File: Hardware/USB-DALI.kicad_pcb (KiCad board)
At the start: 2 copper layers, 71.3 x 25.4 mm, 43 parts, among them J1 USB_A, J2 ST-LINK, J3 Screw_Terminal_01x02, J4 PWR BUS+, J5 PWR BUS-, Q1 BCX56, U1 STM32F103C8T6, U2 PC817, U3 PC817, U4 AMS1117-3.3, U5 MT3608, Y1 8MHz

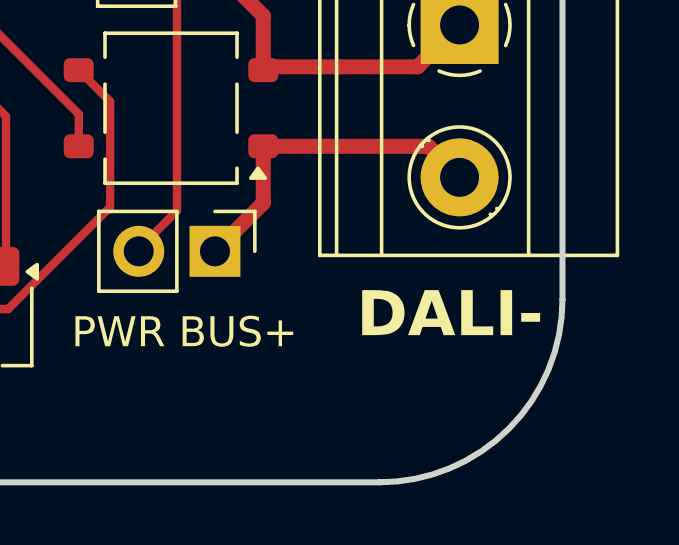
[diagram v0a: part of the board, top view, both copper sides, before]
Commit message: a silk fix & gerbers
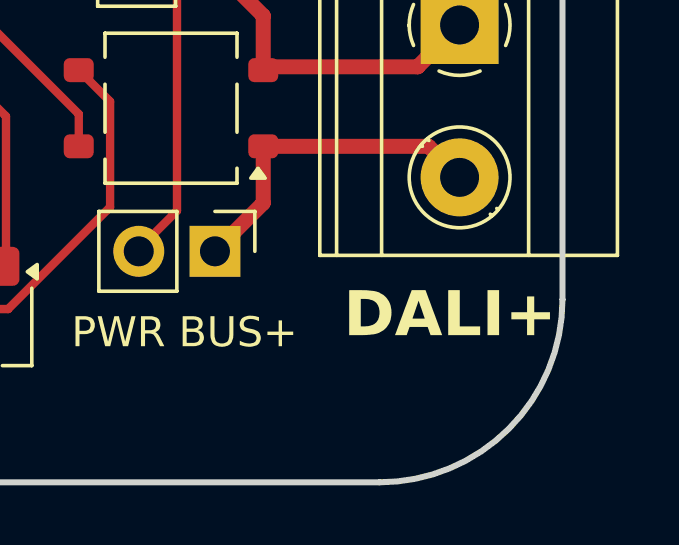
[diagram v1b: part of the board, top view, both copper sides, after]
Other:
- board text added: "DALI+"
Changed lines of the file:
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@@
 			(outputformat 1)
 			(mirror no)
-			(drillshape 1)
+			(drillshape 0)
 			(scaleselection 1)
-			(outputdirectory "")
+			(outputdirectory "Fabrication/")
 		)
 	)
@@
 		)
 	)
-	(gr_text "DALI-"
+	(gr_text "DALI+"
 		(at 188.18 108.125 0)
 		(layer "F.SilkS")
